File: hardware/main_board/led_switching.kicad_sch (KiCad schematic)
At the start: 52 parts, among them Q1 IRF540N, Q10 IRF540N, Q11 IRF540N, Q12 IRF540N, Q13 IRF540N, Q14 IRF540N, Q15 IRF540N, Q16 IRF540N, Q17 IRF540N, Q18 IRF540N, Q19 IRF540N, Q2 IRF540N, Q20 IRF540N, Q21 IRF540N, Q22 IRF540N, Q23 IRF540N, Q24 IRF540N, Q25 IRF540N, Q26 IRF540N, Q27 IRF540N, Q28 IRF540N, Q29 IRF540N, Q3 IRF540N, Q30 IRF540N, Q31 IRF540N, Q32 IRF540N, Q4 IRF540N, Q5 IRF540N, Q6 IRF540N, Q7 IRF540N, Q8 IRF540N, Q9 IRF540N, U16 74HC238, U6 74HC04

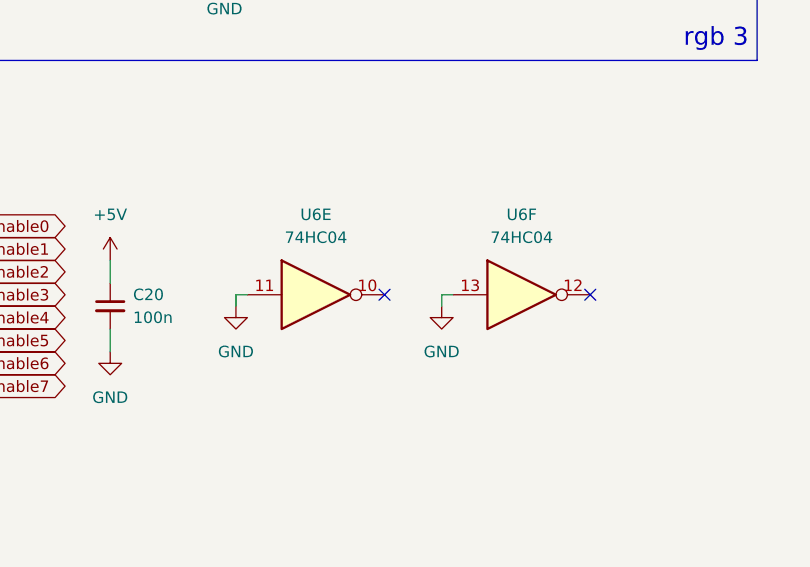
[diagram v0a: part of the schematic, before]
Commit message: #2: Hardware changes to accommodate new standby feature. Might as well commit symbol/footprint tables.
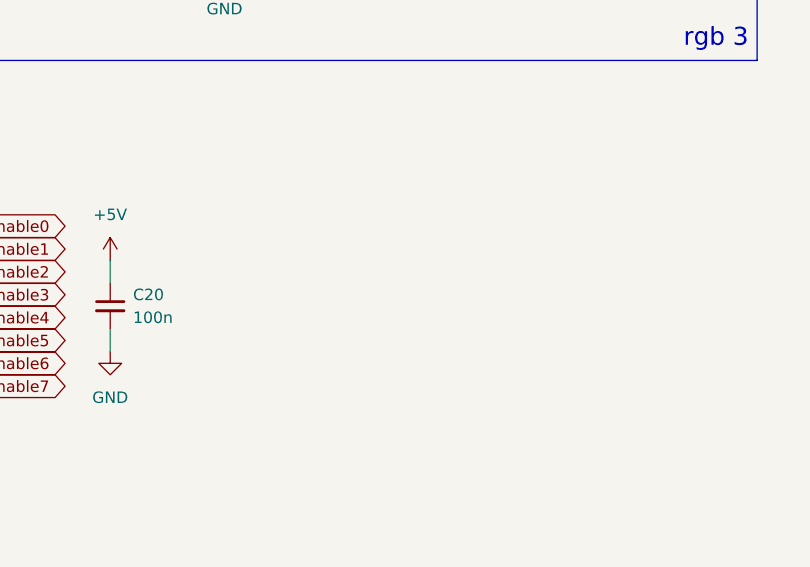
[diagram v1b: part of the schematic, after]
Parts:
- removed unit 5 of U6
- removed unit 6 of U6
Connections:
- no-connect marks 2 -> 0
